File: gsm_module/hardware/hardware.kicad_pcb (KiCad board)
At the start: 2 copper layers, 65 parts, among them J1 Screw_Terminal_01x04, J10 Conn_01x02_Male, J11 Conn_01x02_Male, J12 Conn_01x02_Male, J13 Conn_01x02_Male, J2 78646-3001, J4 Programming interface, J5 SWD Debugging Interface, J6 Conn_01x02_Male, J7 Conn_01x02_Male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

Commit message: PCB rev 0.8
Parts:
- removed C11: 7.5nF, Capacitor_THT:C_Disc_D4.3mm_W1.9mm_P5.00mm
- removed J7: Conn_01x02_Male, Connector_PinHeader_2.54mm:PinHeader_1x02_P2.54mm_Vertical
- removed U7, U8: MOLEX-734120114, its_app:KH-IPEX4-2020
- removed polcap1, polcap3: 470uF, Capacitor_THT:CP_Radial_D8.0mm_P3.50mm
- added A1: BWSMA-KE-Z001, its_app:BWSMA-KE-Z001, F.Cu at (111.0, 61.5)
- added A2: BWSMA-KE-Z001, its_app:BWSMA-KE-Z001, F.Cu at (77.5, 59.0)
- C5: value 7.5nF -> 3.3nF
- moved R17 93.3 mm to (108.5, 69.0), turned to 270 degrees
- moved C15 84.8 mm to (100.5, 60.5), turned to 90 degrees
- moved C14 84.7 mm to (103.0, 60.5), turned to 90 degrees
- moved R10 78.3 mm to (132.5, 125.5), turned to 90 degrees
- moved R9 75.1 mm to (85.0, 55.0)
- moved U6 74.4 mm to (95.5, 73.0), turned to 0 degrees
- moved R1 73.1 mm to (81.0, 141.0)
- moved R13 72.5 mm to (127.5, 112.5), turned to 270 degrees
- moved R3 69.7 mm to (98.5, 136.0), turned to 180 degrees
- moved J12 69.5 mm to (82.5, 66.5), turned to 270 degrees
- moved J2 68.8 mm to (76.0, 82.0)
- moved J1 65.5 mm to (68.0, 117.0)
- moved R8 63.9 mm to (98.0, 59.0)
- moved R12 63.5 mm to (137.0, 113.0), turned to 270 degrees
- moved R14 62.5 mm to (120.0, 101.5), turned to 0 degrees
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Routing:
- net 5v: track 91.6 -> 165.2 mm, vias 2 -> 9
- net 200OK: track 97.0 -> 27.9 mm, vias 2 -> 1
- net CAN-HIGH: track 129.4 -> 64.4 mm
- net NETWORK_ERROR: track 100.2 -> 35.5 mm, vias 2 -> 1
- net CAN-LOW: track 119.8 -> 63.1 mm
- net SIM_CARD_ERROR: track 104.0 -> 47.3 mm, vias 2 -> 1
- net SIM8xx_PWR_PIN: track 25.5 -> 74.7 mm
- net 4v: track 120.4 -> 89.0 mm, vias 3 -> 2
- net 12-40v: track 79.8 -> 106.5 mm
- net STM-SIM8xx_BridgeTX: track 22.6 -> 49.1 mm
- net STM-SIM8xx_BridgeRX: track 31.6 -> 6.69 mm, vias 1 -> 0
- net SIM8xx_GPS_RX: track 32.6 -> 12.5 mm
- net Net-(C10-Pad2): track 89.8 -> 70.9 mm, vias 2 -> 0
- net Net-(R16-Pad1): track 22.7 -> 9.29 mm
- net Net-(R9-Pad1): track 3.92 -> 16.6 mm, vias 0 -> 1
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- added copper zone on B.Cu, net GND
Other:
- board text added: "Rev 0.5 its_app"

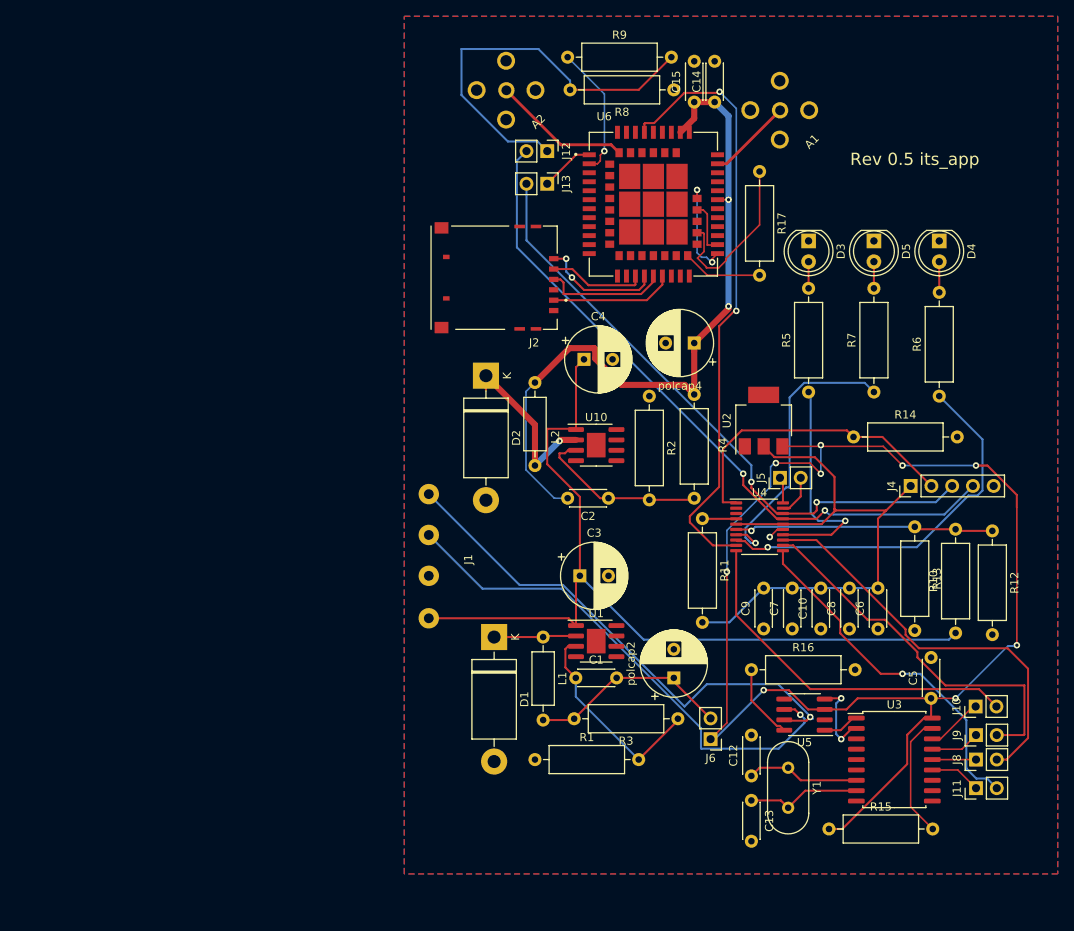
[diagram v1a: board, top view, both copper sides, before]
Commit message: newest PCB no acid traps all up to spec
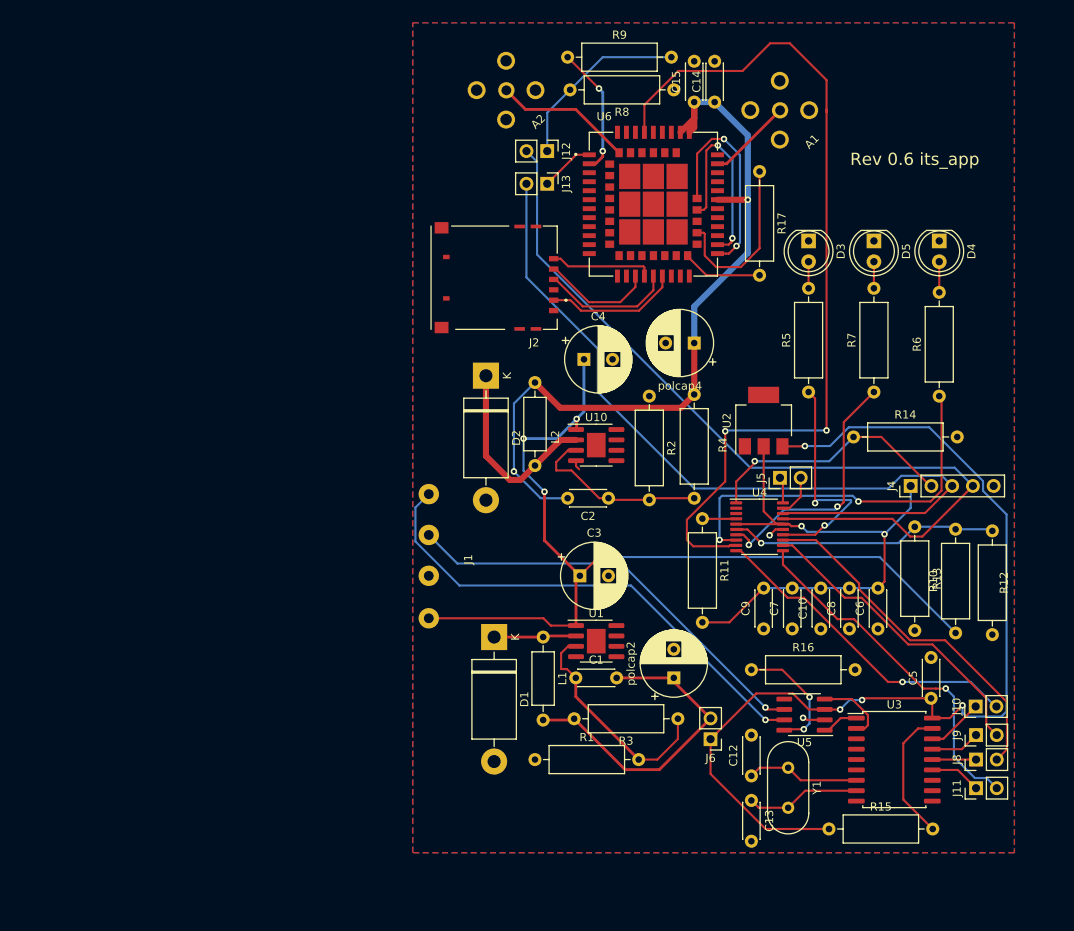
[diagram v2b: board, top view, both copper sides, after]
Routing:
- net 5v: track 165.2 -> 123.9 mm, vias 9 -> 4
- net SIM8xx_PWR_PIN: track 74.7 -> 108.0 mm
- net STM-SIM8xx_BridgeTX: track 49.1 -> 22.7 mm
- net Net-(J13-Pad2): track 76.5 -> 100.9 mm, vias 2 -> 0
- net Net-(J12-Pad2): track 84.8 -> 105.0 mm, vias 2 -> 0
- net SIM8xx_GPS_TX: track 6.53 -> 24.8 mm, vias 0 -> 2
- net Net-(C1-Pad2): track 25.0 -> 39.6 mm
- net SIM8xx_GPS_RX: track 12.5 -> 26.8 mm
- net CAN-LOW: track 63.1 -> 52.4 mm
- net SPI_MISO: track 46.5 -> 37.7 mm
- net 4v: track 89.0 -> 96.1 mm
- net SPI_MOSI: track 50.4 -> 43.6 mm
- net Net-(J4-Pad2): track 37.5 -> 31.4 mm, vias 0 -> 1
- net Net-(R16-Pad1): track 9.29 -> 15.2 mm, vias 0 -> 2
- net 12-40v: track 106.5 -> 111.6 mm, vias 0 -> 4
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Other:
- net class Default: clearance 0.2 -> 0.26; trace_width 0.25 -> 0.25908
- net class small: clearance 0.15 -> 0.26; trace_width 0.2 -> 0.255
- rule trace_clearance: 0.2 -> 0.26
- rule trace_min: 0.2 -> 0.254
- board text added: "Rev 0.6 its_app"
- board text removed: "Rev 0.5 its_app"
